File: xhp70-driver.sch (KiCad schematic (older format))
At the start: 28 parts, among them J1 LEMO2, J2 AVR-ISP-6, Q1 Q_NMOS_GDS, SW1 Rotary_Encoder_Switch, U1 AL8871Q, U2 ATtiny85-20SU, U3 L7805

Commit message: Redo. Same as rev.2b
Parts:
- U3: symbol Regulator_Linear:L7805 -> Regulator_Linear:AP2127N-3.0
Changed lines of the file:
@@
 $EndComp
 $Comp
-L Regulator_Linear:L7805 U3
+L Regulator_Linear:AP2127N-3.0 U3
 U 1 1 6039EB96
 P 1800 5650

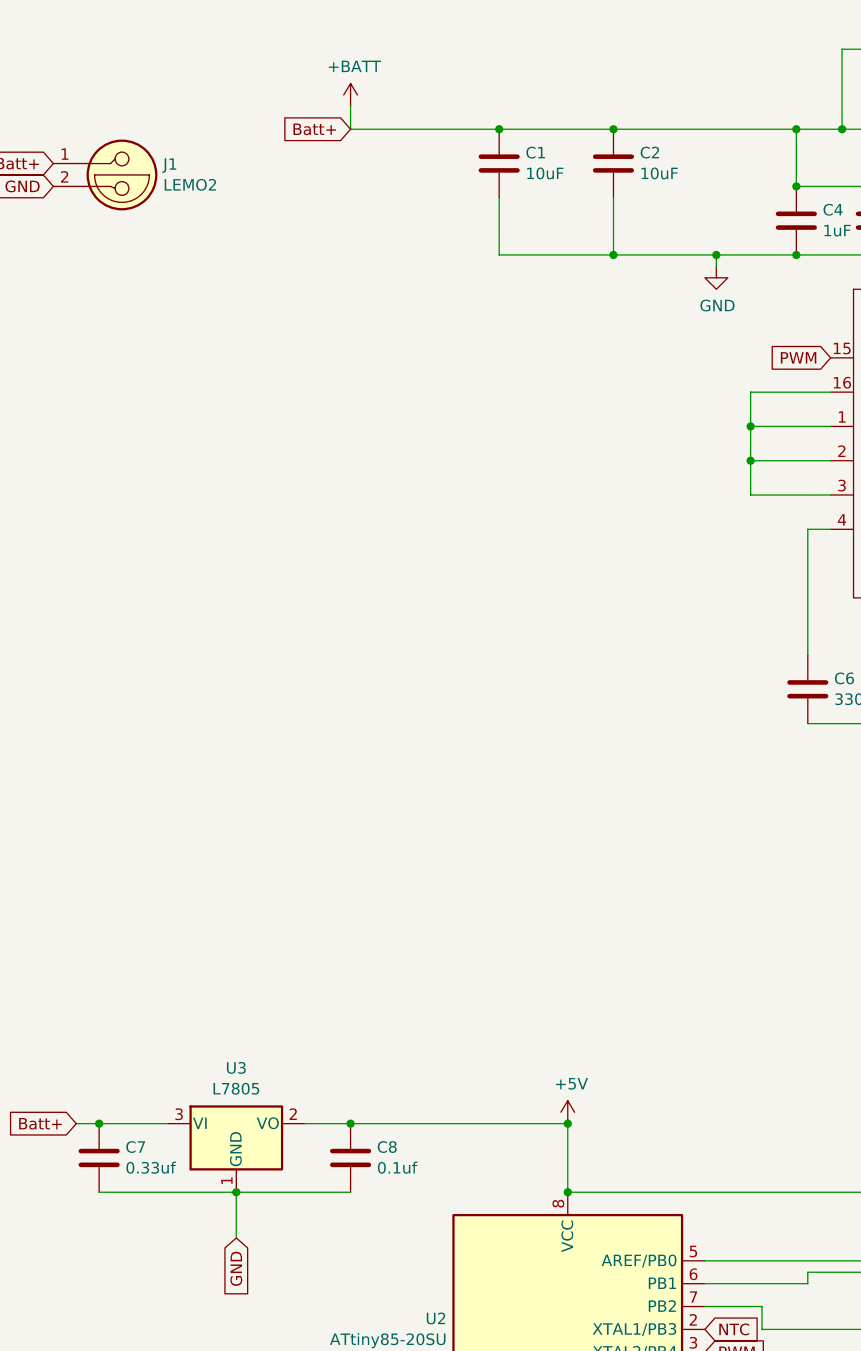
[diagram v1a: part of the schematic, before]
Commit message: Changed LDO to 78L05 linear voltage regulator
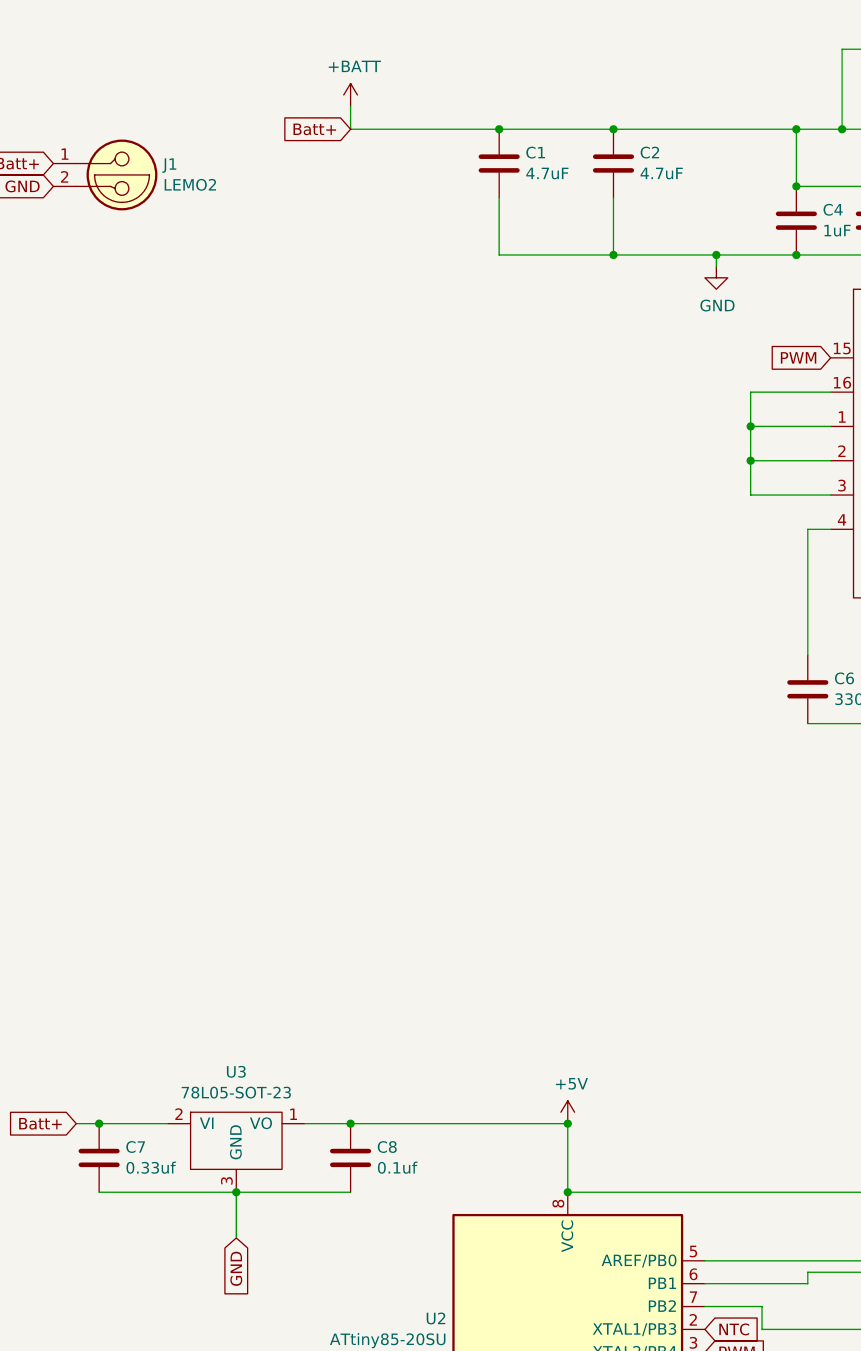
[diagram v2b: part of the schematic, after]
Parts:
- removed U3: L7805, Package_TO_SOT_SMD:SOT-23, symbol Regulator_Linear:AP2127N-3.0
- added U3: 78L05-SOT-23, Package_TO_SOT_SMD:SOT-23, symbol LED-driver:78L05-SOT-23
- C1, C2: value 10uF -> 4.7uF
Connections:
- net +5V: now also U3.1 (VO)
- net +BATT: now also U3.2 (VI)
- net GND: now also U3.3 (GND)
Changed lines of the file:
@@
 P 2950 1450
 F 0 "C1" H 3065 1496 50  0000 L CNN
-F 1 "10uF" H 3065 1405 50  0000 L CNN
+F 1 "4.7uF" H 3065 1405 50  0000 L CNN
 F 2 "Capacitor_SMD:C_1206_3216Metric_Pad1.33x1.80mm_HandSolder" H 2988 1300 50  0001 C CNN
 F 3 "~" H 2950 1450 50  0001 C CNN
@@
 	1    0    0    -1
 $EndComp
-$Comp
-L Regulator_Linear:AP2127N-3.0 U3
-U 1 1 6039EB96
-P 1800 5650
-F 0 "U3" H 1800 5892 50  0000 C CNN
-F 1 "L7805" H 1800 5801 50  0000 C CNN
-F 2 "Package_TO_SOT_SMD:SOT-23" H 1825 5500 50  0001 L CIN
-F 3 "http://www.st.com/content/ccc/resource/technical/document/datasheet/41/4f/b3/b0/12/d4/47/88/CD00000444.pdf/files/CD00000444.pdf/jcr:content/translations/en.CD00000444.pdf" H 1800 5600 50  0001 C CNN
-	1    1800 5650
-	1    0    0    -1
-$EndComp
 Text GLabel 4400 2300 0    50   Input ~ 0
 PWM
@@
 P 3450 1450
 F 0 "C2" H 3565 1496 50  0000 L CNN
-F 1 "10uF" H 3565 1405 50  0000 L CNN
+F 1 "4.7uF" H 3565 1405 50  0000 L CNN
 F 2 "Capacitor_SMD:C_1206_3216Metric_Pad1.33x1.80mm_HandSolder" H 3488 1300 50  0001 C CNN
 F 3 "~" H 3450 1450 50  0001 C CNN
@@
 EC_B
 $Comp
-L power:GND #PWR?
+L power:GND #PWR0106
 U 1 1 604E195D
 P 6350 5500
-F 0 "#PWR?" H 6350 5250 50  0001 C CNN
+F 0 "#PWR0106" H 6350 5250 50  0001 C CNN
 F 1 "GND" H 6355 5327 50  0000 C CNN
 F 2 "" H 6350 5500 50  0001 C CNN
@@
 $EndComp
 $Comp
-L power:GND #PWR?
+L power:GND #PWR0107
 U 1 1 604F3390
 P 7350 6000
-F 0 "#PWR?" H 7350 5750 50  0001 C CNN
+F 0 "#PWR0107" H 7350 5750 50  0001 C CNN
 F 1 "GND" H 7355 5827 50  0000 C CNN
 F 2 "" H 7350 6000 50  0001 C CNN
@@
 $EndComp
 $Comp
-L power:GND #PWR?
+L power:GND #PWR0108
 U 1 1 604F37B3
 P 8750 6100
-F 0 "#PWR?" H 8750 5850 50  0001 C CNN
+F 0 "#PWR0108" H 8750 5850 50  0001 C CNN
 F 1 "GND" H 8755 5927 50  0000 C CNN
 F 2 "" H 8750 6100 50  0001 C CNN
@@
 	1    0    0    -1
 $EndComp
+$Comp
+L LED-driver:78L05-SOT-23 U3
+U 1 1 60811EC2
+P 1800 5500
+F 0 "U3" H 1800 5575 50  0000 C CNN
+F 1 "78L05-SOT-23" H 1800 5484 50  0000 C CNN
+F 2 "Package_TO_SOT_SMD:SOT-23" H 1800 5500 50  0001 C CNN
+F 3 "" H 1800 5500 50  0001 C CNN
+	1    1800 5500
+	1    0    0    -1
+$EndComp
